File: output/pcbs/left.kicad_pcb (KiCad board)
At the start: 2 copper layers, 140.2 x 118.9 mm, 62 parts

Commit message: A bit more touch-up on the PCB.  Things are shaping up, but not yet done.
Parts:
- added ROT1: , rotary_encoder, F.Cu at (213.0, 70.5)
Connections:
- D28 pad 1: (no net) -> P113
- D29 pad 1: (no net) -> P113
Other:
- board text added: "CYBERFOX-60"
- board text removed: "CYBERFOX"

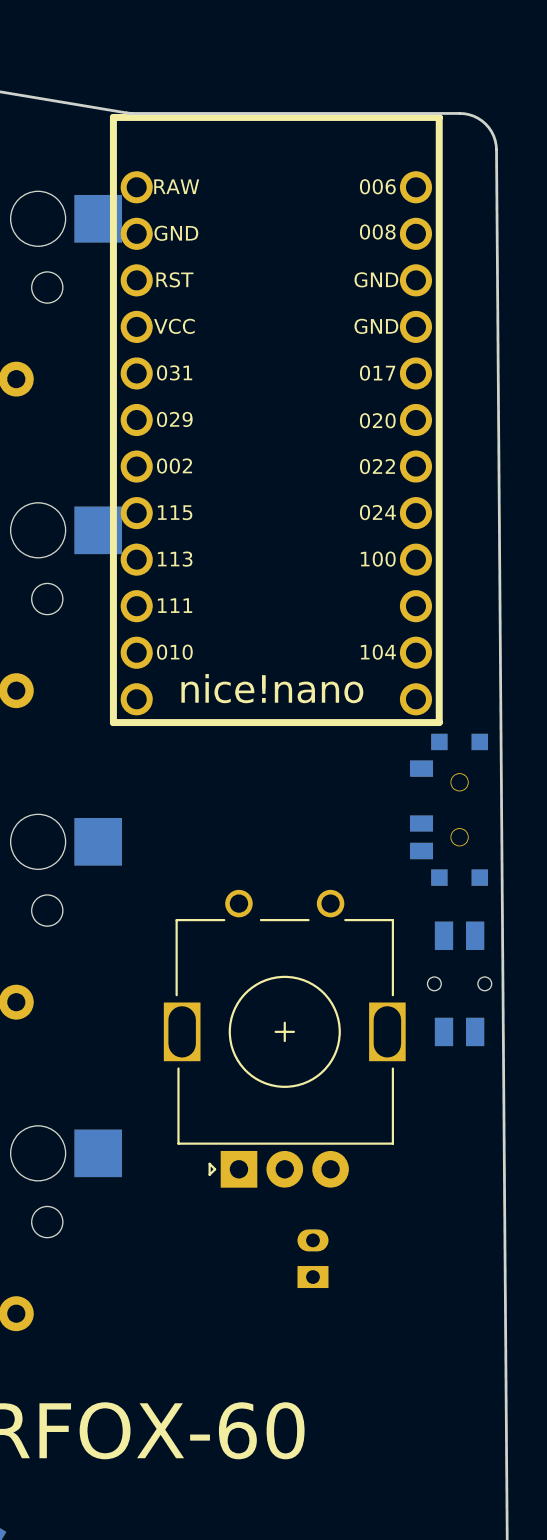
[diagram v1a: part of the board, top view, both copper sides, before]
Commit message: Changed from rotary knob to scrollwheel. Further minor refinements.
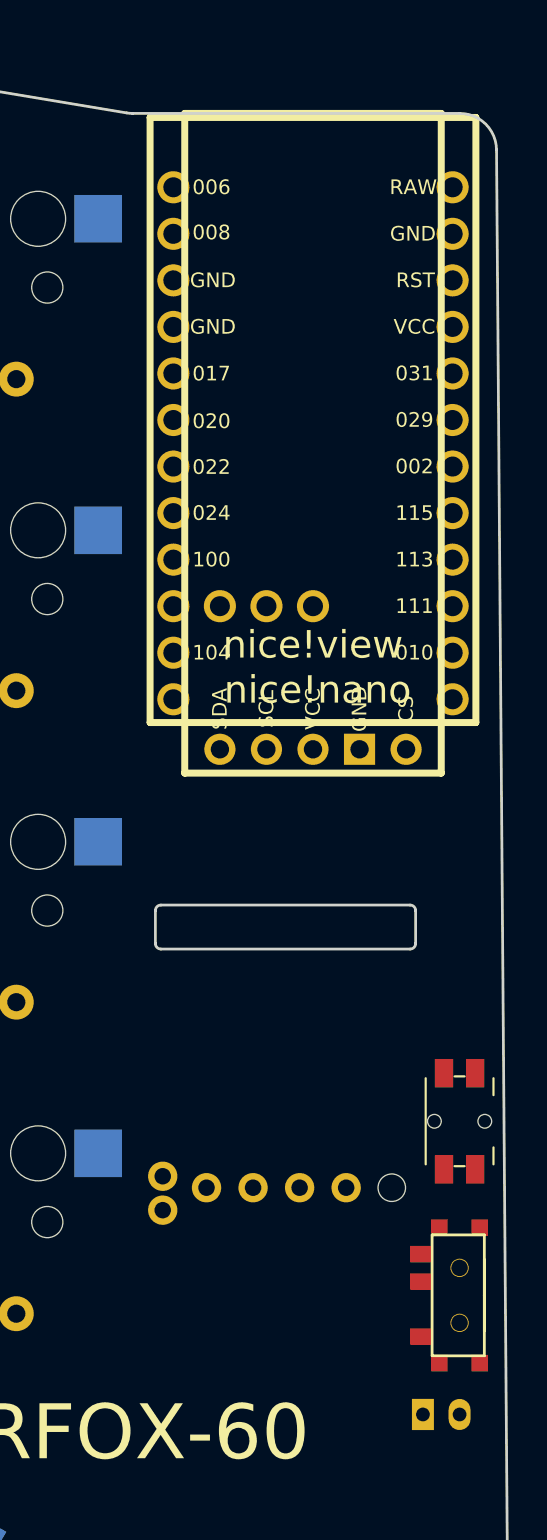
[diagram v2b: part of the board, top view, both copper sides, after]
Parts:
- removed ROT1: , rotary_encoder
- added REF**: RollerEncoder_Panasonic_EVQWGD001, RollerEncoder_Panasonic_EVQWGD001, F.Cu at (212.5, 73.5)
- added niceView1: niceView, lib:niceView_headers, F.Cu at (214.5, 56.5)
- moved T1 26.5 mm to (222.5, 85.0)
- moved JST1 11.0 mm to (221.5, 91.5), turned to 0 degrees
- moved B1 7.50 mm to (222.5, 75.5)
- moved MCU1 2.00 mm to (214.5, 38.5)
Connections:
- net pos renamed POS
- D13 pad 1: P013 -> P031
- D18 pad 1: P013 -> P031
- D23 pad 1: P013 -> P031
- D27 pad 1: P013 -> P031
- D4 pad 1: P013 -> P031
- D8 pad 1: P013 -> P031
- S1 pad 1: P020 -> P011
- S10 pad 1: P024 -> P106
- S11 pad 1: P024 -> P106
- S12 pad 1: P024 -> P106
- S13 pad 1: P024 -> P106
- S14 pad 1: P024 -> P106
- S15 pad 1: P100 -> P111
- S16 pad 1: P100 -> P111
- S17 pad 1: P100 -> P111
- S18 pad 1: P100 -> P111
- S19 pad 1: P100 -> P111
- S2 pad 1: P020 -> P011
- S20 pad 1: P011 -> P010
- S21 pad 1: P011 -> P010
- S22 pad 1: P011 -> P010
- S23 pad 1: P011 -> P010
- S24 pad 1: P017 -> P009
- S25 pad 1: P017 -> P009
- S26 pad 1: P017 -> P009
- S27 pad 1: P017 -> P009
- S28 pad 1: P011 -> P010
- S29 pad 1: P017 -> P009
- S3 pad 1: P020 -> P011
- S4 pad 1: P020 -> P011
- S5 pad 1: P022 -> P104
- S6 pad 1: P022 -> P104
- S7 pad 1: P022 -> P104
- S8 pad 1: P022 -> P104
- S9 pad 1: P022 -> P104

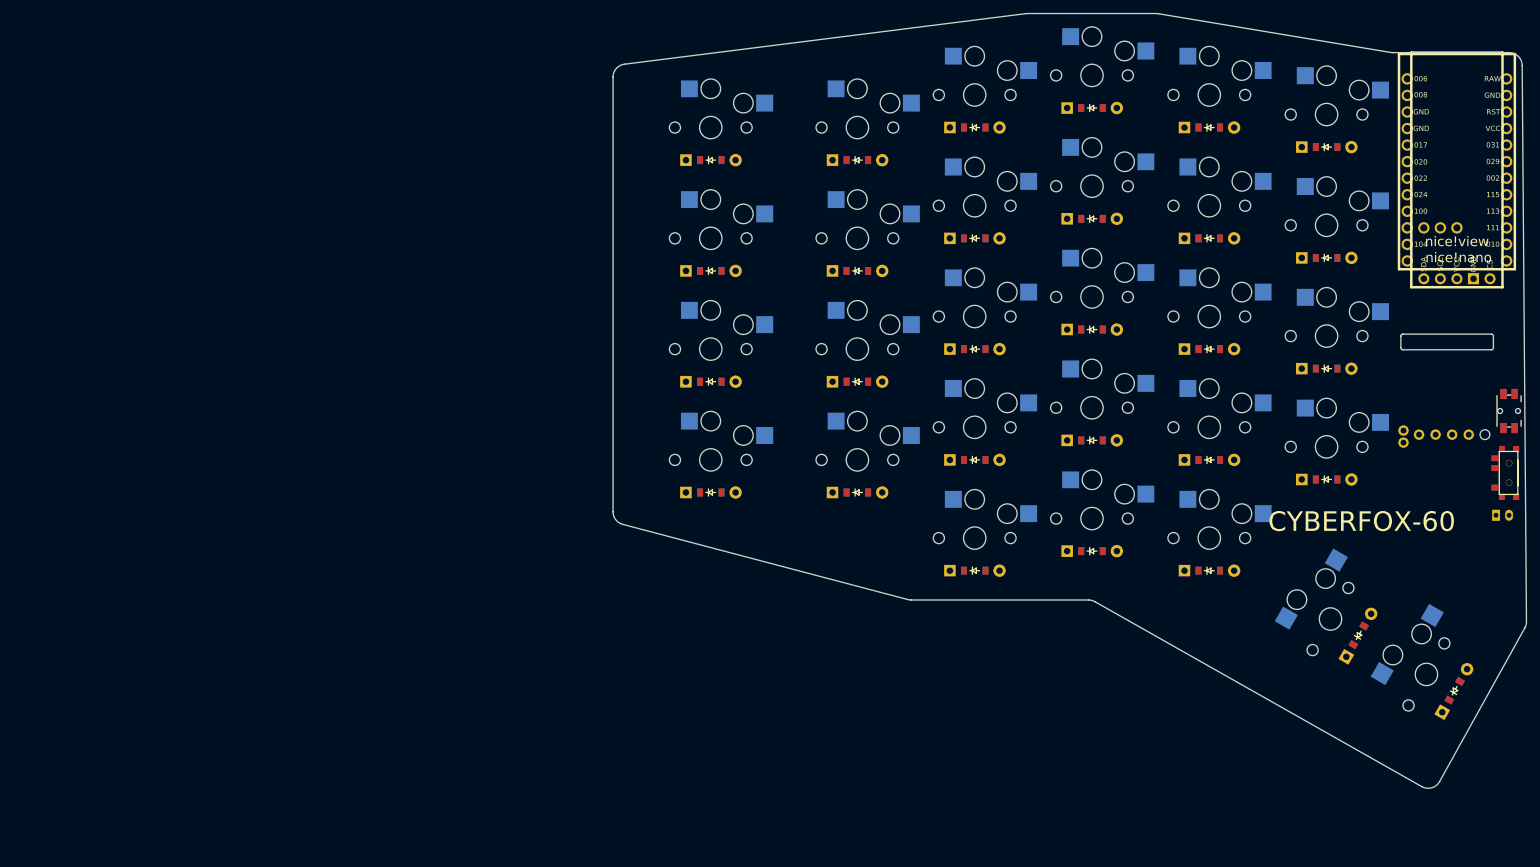
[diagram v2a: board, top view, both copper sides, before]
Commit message: Added screw holes and an extra diode for the scrollwheel
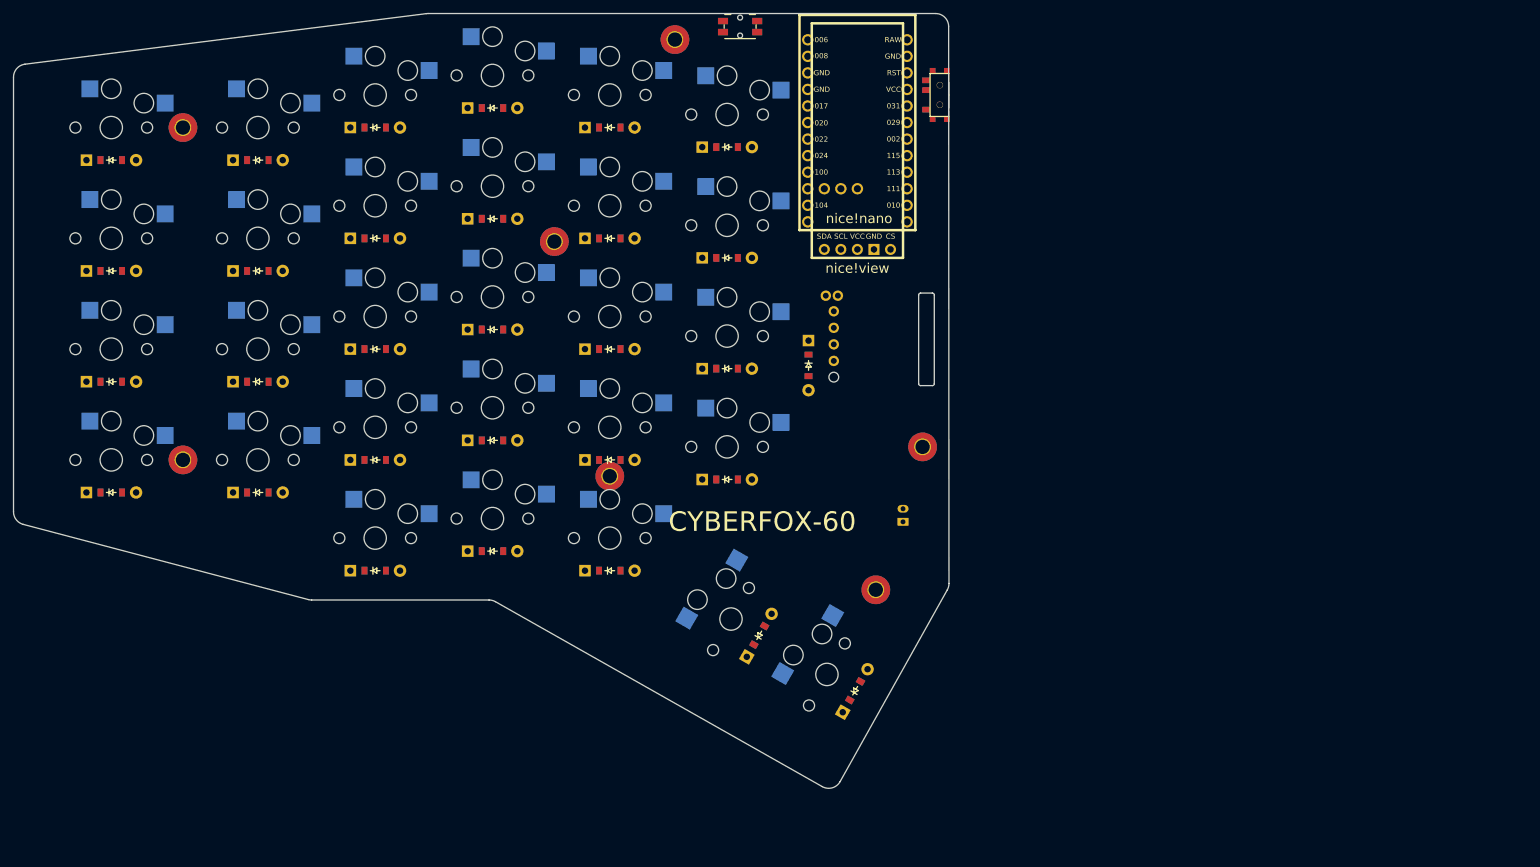
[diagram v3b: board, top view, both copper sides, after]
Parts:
- added D30: , ComboDiode, F.Cu at (115.0, 68.5)
- added _2: , HOLE_M2, F.Cu at (125.3, 102.9)
- added _3: , HOLE_M2, F.Cu at (132.5, 81.0)
- added _4: , HOLE_M2, F.Cu at (94.5, 18.5)
- added _5: , HOLE_M2, F.Cu at (19.0, 32.0)
- added _6: , HOLE_M2, F.Cu at (19.0, 83.0)
- added _7: , HOLE_M2, F.Cu at (76.0, 49.5)
- added _8: , HOLE_M2, F.Cu at (84.5, 85.5)
- REF**: value RollerEncoder_Panasonic_EVQWGD001 -> EVQWGD001
- moved B1 131.9 mm to (104.5, 16.5), turned to 0 degrees
- moved T1 104.9 mm to (135.2, 27.0)
- moved MCU1 92.2 mm to (122.5, 32.5)
- moved niceView1 92.1 mm to (122.5, 52.0)
- moved D1 92.0 mm to (8.00, 88.0)
- moved D10 92.0 mm to (48.5, 83.0)
- moved D11 92.0 mm to (48.5, 66.0)
- moved D12 92.0 mm to (48.5, 49.0)
- moved D13 92.0 mm to (48.5, 32.0)
- moved D14 92.0 mm to (66.5, 97.0)
- moved D15 92.0 mm to (66.5, 80.0)
- moved D16 92.0 mm to (66.5, 63.0)
- moved D17 92.0 mm to (66.5, 46.0)
- moved D18 92.0 mm to (66.5, 29.0)
- moved D19 92.0 mm to (84.5, 100.0)
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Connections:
- REF** pad S2: P113 -> ROTARY
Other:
- board size 140.2 x 118.9 mm -> 143.6 x 118.9 mm

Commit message: Starting to trace the PCB
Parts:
- moved _8 46.2 mm to (118.8, 116.5)
- moved B1 38.1 mm to (141.5, 25.5)
- moved _4 36.9 mm to (130.8, 25.5)
- moved D28 36.4 mm to (142.4, 119.9)
- moved S28 36.4 mm to (138.1, 117.4)
- moved _2 36.4 mm to (160.3, 112.9)
- moved D29 36.4 mm to (157.2, 128.4)
- moved S29 36.4 mm to (152.8, 125.9)
- moved D24 36.2 mm to (137.5, 95.2)
- moved JST1 36.2 mm to (164.5, 100.8)
- moved MCU1 36.2 mm to (157.5, 41.8)
- moved S24 36.2 mm to (137.5, 90.2)
- moved _3 36.2 mm to (167.5, 90.2)
- moved niceView1 36.2 mm to (157.5, 61.2)
- moved D25 36.0 mm to (137.5, 77.5)
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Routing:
- net P011: track 0.00 -> 291.2 mm
- net P113: track 0.00 -> 213.5 mm
- net P115: track 0.00 -> 207.8 mm
- net P031: track 0.00 -> 193.2 mm
- net P002: track 0.00 -> 193.0 mm
- net P029: track 0.00 -> 178.5 mm
- net GND: track 0.00 -> 113.5 mm
- net P010: track 0.00 -> 108.5 mm
- net P009: track 0.00 -> 106.5 mm
- net P111: track 0.00 -> 96.0 mm
- net P106: track 0.00 -> 92.6 mm
- net P104: track 0.00 -> 91.2 mm
- net POS: track 0.00 -> 72.5 mm
- net P017: track 0.00 -> 35.0 mm, vias 0 -> 1
- net RST: track 0.00 -> 32.9 mm
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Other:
- board size 143.6 x 118.9 mm -> 149.1 x 121.9 mm
- net class Default removed

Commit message: Slow progress on routing the connections on the left PCB.
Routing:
- net P104: track 91.2 -> 227.6 mm
- net P106: track 92.6 -> 209.9 mm
- net P111: track 96.0 -> 197.7 mm
- net P010: track 108.5 -> 147.6 mm
- net P011: track 291.2 -> 274.7 mm

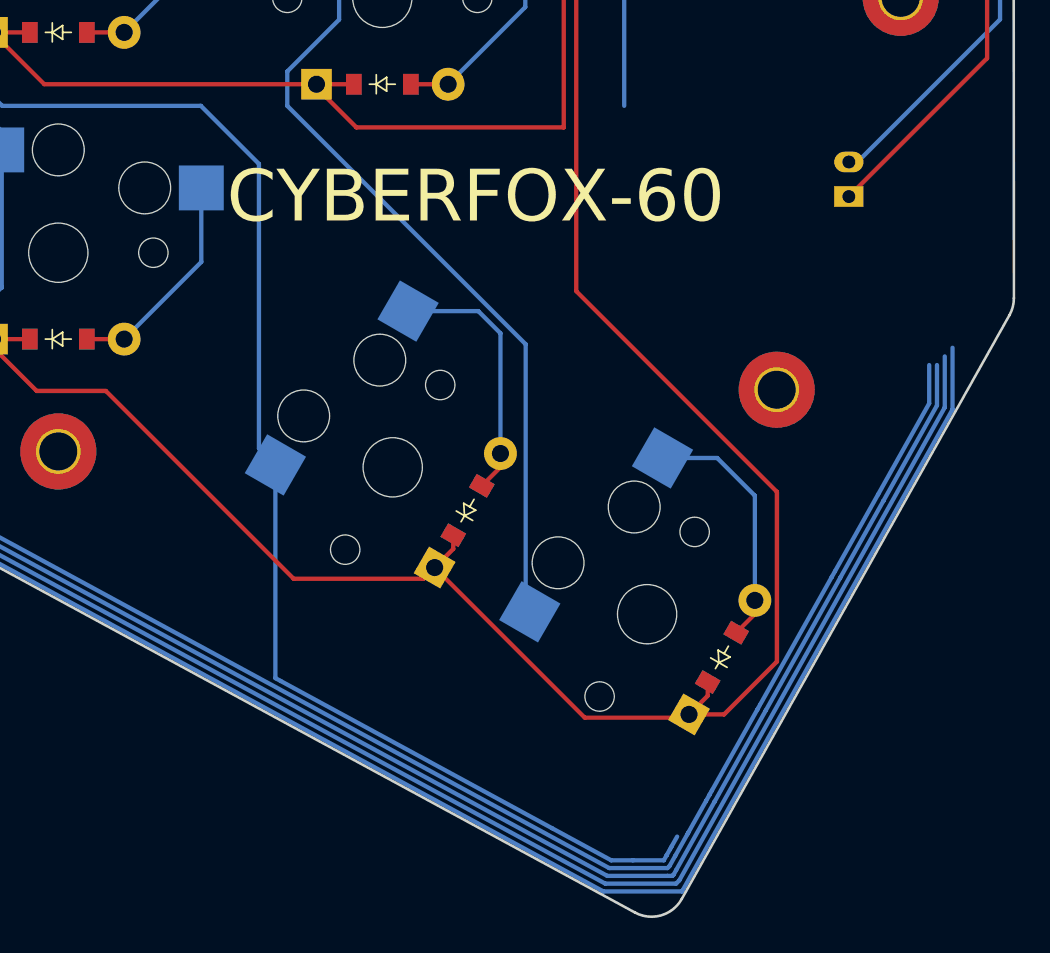
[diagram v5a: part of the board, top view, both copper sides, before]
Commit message: Got the columns routed around the thumb cluster on the left PCB
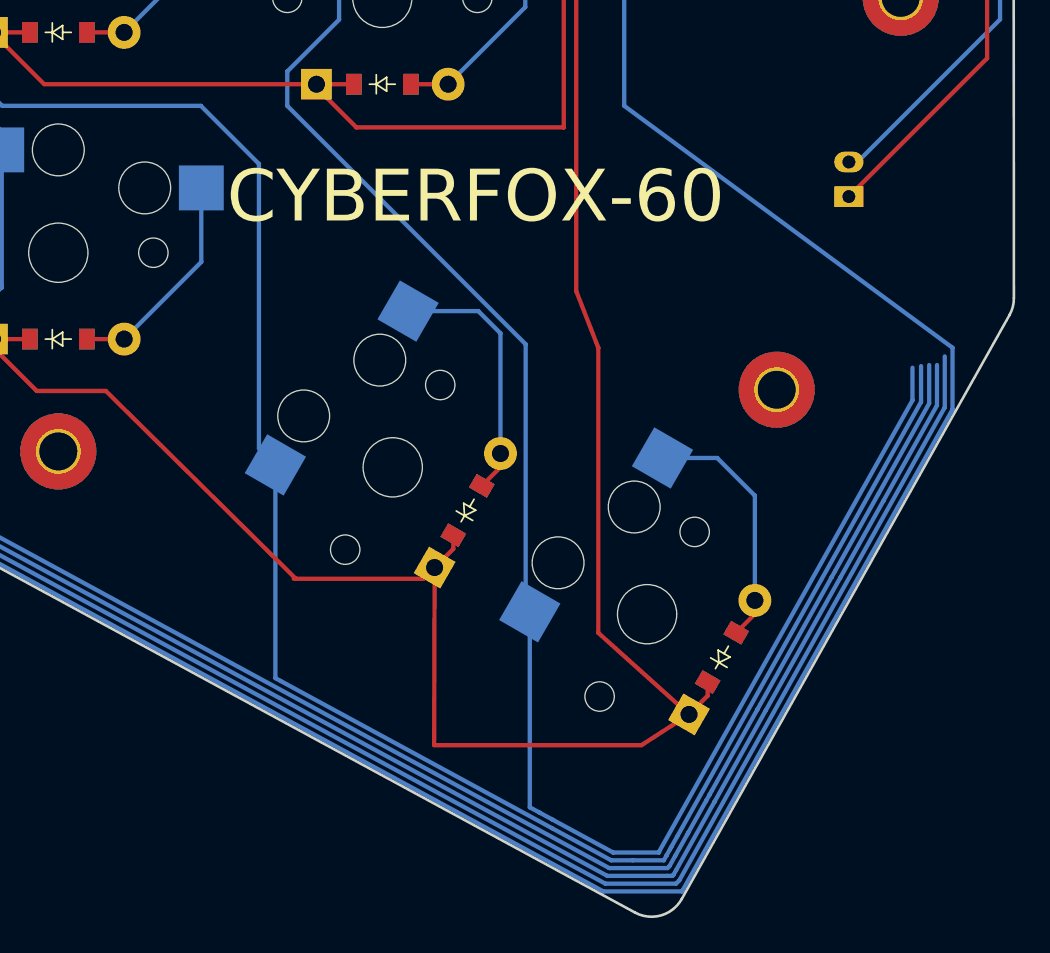
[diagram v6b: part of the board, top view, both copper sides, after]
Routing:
- net P009: track 106.5 -> 157.8 mm
- net P010: track 147.6 -> 178.5 mm
- net P011: track 274.7 -> 298.3 mm
- net P113: track 213.5 -> 215.5 mm
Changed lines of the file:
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@@
 	)
 	(segment
+		(start 170.5 110.5)
+		(end 151.5 96.5)
+		(width 0.25)
+		(layer "B.Cu")
+		(net 1)
+	)
+	(segment
 		(start 170.5 114.073741)
 		(end 170.5 110.5)
@@
 	)
 	(segment
+		(start 154.562606 138.789937)
+		(end 168.678513 113.635376)
+		(width 0.25)
+		(layer "B.Cu")
+		(net 24)
+	)
+	(segment
 		(start 113.726 55.536)
 		(end 113.726 61.801)
@@
 	)
 	(segment
+		(start 168.678513 113.635376)
+		(end 168.678513 111.561577)
+		(width 0.25)
+		(layer "B.Cu")
+		(net 24)
+	)
+	(segment
 		(start 130.360547 116.329998)
 		(end 131.312213 117.281664)
@@
 	)
 	(segment
+		(start 153.51366 139.670606)
+		(end 168.183192 113.542647)
+		(width 0.25)
+		(layer "B.Cu")
+		(net 29)
+	)
+	(segment
+		(start 146.597032 137.399527)
+		(end 147.37006 137.818912)
+		(width 0.25)
+		(layer "B.Cu")
+		(net 29)
+	)
+	(segment
 		(start 134.225 56.787)
 		(end 132.476 58.536)
@@
 	)
 	(segment
+		(start 168.183192 113.542647)
+		(end 168.183192 111.654327)
+		(width 0.25)
+		(layer "B.Cu")
+		(net 29)
+	)
+	(segment
+		(start 150.862119 139.713435)
+		(end 153.51366 139.713435)
+		(width 0.25)
+		(layer "B.Cu")
+		(net 29)
+	)
+	(segment
 		(start 134.225 84.3)
 		(end 135 85.075)
@@
 	)
 	(segment
+		(start 146.034644 137.094418)
+		(end 146.597032 137.399527)
+		(width 0.25)
+		(layer "B.Cu")
+		(net 29)
+	)
+	(segment
 		(start 132.476 58.536)
 		(end 132.476 64.801)
@@
 	)
 	(segment
+		(start 147.37006 137.818912)
+		(end 150.862119 139.713435)
+		(width 0.25)
+		(layer "B.Cu")
+		(net 29)
+	)
+	(segment
 		(start 132 94.512)
 		(end 132 96.5)
@@
 	)
 	(segment
+		(start 153.51366 139.713435)
+		(end 153.51366 139.670606)
+		(width 0.25)
+		(layer "B.Cu")
+		(net 29)
+	)
+	(segment
 		(start 132.476 40.786)
 		(end 132.476 47.051)
@@
 	)
 	(segment
+		(start 146.034644 125.781664)
+		(end 146.034644 137.094418)
+		(width 0.25)
+		(layer "B.Cu")
+		(net 29)
+	)
+	(segment
 		(start 141.31 95.25)
 		(end 139.15 95.25)
@@
 	)
 	(segment
-		(start 149.217174 131.909471)
-		(end 140.527691 123.219988)
-		(width 0.25)
-		(layer "F.Cu")
-		(net 40)
-	)
-	(segment
 		(start 117.1 110)
 		(end 114.94 110)
@@
 	)
 	(segment
-		(start 155.060639 131.909471)
-		(end 149.217174 131.909471)
-		(width 0.25)
-		(layer "F.Cu")
-		(net 40)
-	)
-	(segment
 		(start 79.94 112.5)
 		(end 77.44 110)
@@
 	)
 	(segment
-		(start 139.876898 123.870781)
-		(end 132.370781 123.870781)
+		(start 140.5 133.5)
+		(end 152.5 133.5)
 		(width 0.25)
 		(layer "F.Cu")
@@
 	)
 	(segment
-		(start 163.309188 56.9)
-		(end 161.9 55.490812)
-		(width 0.25)
-		(layer "F.Cu")
-		(net 40)
-	)
-	(segment
-		(start 160.337622 118.837622)
-		(end 148.7225 107.2225)
+		(start 132.5 123.870781)
+		(end 132.370781 123.870781)
 		(width 0.25)
 		(layer "F.Cu")
@@
 	)
 	(segment
-		(start 132.370781 123.870781)
-		(end 121.5 113)
+		(start 163.309188 56.9)
+		(end 161.9 55.490812)
 		(width 0.25)
 		(layer "F.Cu")
@@
 	)
 	(segment
-		(start 98.35 107)
-		(end 96.19 107)
+		(start 155.250122 131.719988)
+		(end 150 127)
 		(width 0.25)
 		(layer "F.Cu")
@@
 	)
 	(segment
-		(start 157.280012 131.719988)
-		(end 160.337622 128.662378)
+		(start 150 110.5)
+		(end 148.7225 107.2225)
+		(width 0.25)
+		(layer "F.Cu")
+		(net 40)
+	)
+	(segment
+		(start 98.35 107)
+		(end 96.19 107)
 		(width 0.25)
 		(layer "F.Cu")
@@
 	)
 	(segment
+		(start 152.5 133.5)
+		(end 155.250122 131.719988)
+		(width 0.25)
+		(layer "F.Cu")
+		(net 40)
+	)
+	(segment
+		(start 139.876898 123.870781)
+		(end 132.5 123.870781)
+		(width 0.25)
+		(layer "F.Cu")
+		(net 40)
+	)
+	(segment
 		(start 141.607691 122.139988)
 		(end 140.527691 123.219988)
@@
 	)
 	(segment
-		(start 155.250122 131.719988)
-		(end 157.280012 131.719988)
-		(width 0.25)
-		(layer "F.Cu")
-		(net 40)
-	)
-	(segment
 		(start 165.555 61.182285)
 		(end 165.555 58.717715)
@@
 	(segment
 		(start 140.527691 123.219988)
+		(end 140.5 133.5)
+		(width 0.25)
+		(layer "F.Cu")
+		(net 40)
+	)
+	(segment
+		(start 140.527691 123.219988)
 		(end 139.876898 123.870781)
 		(width 0.25)
@@
 	)
 	(segment
+		(start 121.5 113)
+		(end 132.5 123.870781)
+		(width 0.25)
+		(layer "F.Cu")
+		(net 40)
+	)
+	(segment
 		(start 161.9 51.32)
 		(end 165.12 48.1)
@@
 	)
 	(segment
-		(start 160.337622 128.662378)
-		(end 160.337622 118.837622)
-		(width 0.25)
-		(layer "F.Cu")
-		(net 40)
-	)
-	(segment
 		(start 96 107)
 		(end 90.5 112.5)
@@
 		(width 0.25)
 		(layer "F.Cu")
+		(net 40)
+	)
+	(segment
+		(start 150 127)
+		(end 150 110.5)
+		(width 0.25)
+		(layer "F.Cu")
